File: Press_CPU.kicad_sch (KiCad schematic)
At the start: 97 parts, among them J1 Conn_01x02, J2 2-215079-0, U1 APM32F405RGT6, U10 LMV321, U11 LMV321, U12 FM25W256, U13 LMV321, U14 LMV321, U15 LMV321, U16 LMV321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

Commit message: VER1.0: добавил гребенку
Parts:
- added J3, J4: Conn_01x16, PLD_my:PLD16_2.0mm, symbol Connector_Generic:Conn_01x16
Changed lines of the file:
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@@
+	)
+	(symbol
+		(lib_id "Connector_Generic:Conn_01x16")
+		(at 66.04 214.63 0)
+		(unit 1)
+		(exclude_from_sim no)
+		(in_bom yes)
+		(on_board yes)
+		(dnp no)
+		(fields_autoplaced yes)
+		(property "Reference" "J3"
+			(at 68.58 214.63 0)
+			(effects
+				(font
+					(size 1.27 1.27)
+				)
+				(justify left)
+			)
+		)
+		(property "Value" "Conn_01x16"
+			(at 68.58 217.17 0)
+			(effects
+				(font
+					(size 1.27 1.27)
+				)
+				(justify left)
+			)
+		)
+		(property "Footprint" "PLD_my:PLD16_2.0mm"
+			(at 66.04 214.63 0)
+			(effects
+				(font
+					(size 1.27 1.27)
+				)
+				(hide yes)
+			)
+		)
+		(property "Datasheet" "~"
+			(at 66.04 214.63 0)
+			(effects
+				(font
+					(size 1.27 1.27)
+				)
+				(hide yes)
+			)
+		)
+		(property "Description" "Generic connector, single row, 01x16, script generated (kicad-library-utils/schlib/autogen/connector/)"
+			(at 66.04 214.63 0)
+			(effects
+				(font
+					(size 1.27 1.27)
+				)
+				(hide yes)
+			)
+		)
+		(pin "6"
+		)
+		(pin "9"
+		)
+		(pin "2"
+		)
+		(pin "5"
+		)
+		(pin "14"
+		)
+		(pin "16"
+		)
+		(pin "13"
+		)
+		(pin "1"
+		)
+		(pin "4"
+		)
+		(pin "12"
+		)
+		(pin "15"
+		)
+		(pin "3"
+		)
+		(pin "10"
+		)
+		(pin "7"
+		)
+		(pin "11"
+		)
+		(pin "8"
+		)
+		(instances
+			(project ""
+				(path "/1f44d793-713f-4781-bd7e-20142de81965"
+					(reference "J3")
+					(unit 1)
+				)
+			)
+		)
 	)
 	(symbol
@@
 					(unit 1)
 				)
+			)
+		)
+	)
+	(symbol
+		(lib_id "Connector_Generic:Conn_01x16")
+		(at 83.82 214.63 0)
+		(unit 1)
+		(exclude_from_sim no)
+		(in_bom yes)
+		(on_board yes)
+		(dnp no)
+		(fields_autoplaced yes)
+		(property "Reference" "J4"
+			(at 86.36 214.63 0)
+			(effects
+				(font
+					(size 1.27 1.27)
+				)
+				(justify left)
+			)
+		)
+		(property "Value" "Conn_01x16"
+			(at 86.36 217.17 0)
+			(effects
+				(font
+					(size 1.27 1.27)
+				)
+				(justify left)
+			)
+		)
+		(property "Footprint" "PLD_my:PLD16_2.0mm"
+			(at 83.82 214.63 0)
+			(effects
+				(font
+					(size 1.27 1.27)
+				)
+				(hide yes)
+			)
+		)
+		(property "Datasheet" "~"
+			(at 83.82 214.63 0)
+			(effects
+				(font
+					(size 1.27 1.27)
+				)
+				(hide yes)
+			)
+		)
+		(property "Description" "Generic connector, single row, 01x16, script generated (kicad-library-utils/schlib/autogen/connector/)"
+			(at 83.82 214.63 0)
+			(effects
+				(font
+					(size 1.27 1.27)
+				)
+				(hide yes)
+			)
+		)
+		(pin "6"
+		)
+		(pin "9"
+		)
+		(pin "2"
+		)
+		(pin "5"
+		)
+		(pin "14"
+		)
+		(pin "16"
+		)
+		(pin "13"
+		)
+		(pin "1"
+		)
+		(pin "4"
+		)
+		(pin "12"
+		)
+		(pin "15"
+		)
+		(pin "3"
+		)
+		(pin "10"
+		)
+		(pin "7"
+		)
+		(pin "11"
+		)
+		(pin "8"
+		)
+		(instances
+			(project "Press_CPU"
+				(path "/1f44d793-713f-4781-bd7e-20142de81965"
+					(reference "J4")
+					(unit 1)
+				)

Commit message: VER1.0: добавил в разъём сигналы
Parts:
- removed J1: Conn_01x02, Wire_my:Wire_1.5mm, symbol Connector_Generic:Conn_01x02
- added C40: 1n, Capacitor_SMD:C_0603_1608Metric_Pad1.08x0.95mm_HandSolder, symbol Device:C_Small
- added R37, R66: 3.6k, Resistor_SMD:R_0603_1608Metric_Pad0.98x0.95mm_HandSolder, symbol Device:R_Small
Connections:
- net +5V: now also J3.10 (Pin_10), J4.7 (Pin_7)
- net CANH: now also J2.7
- net CANL: now also J2.6
- net Current_A: now also J3.5 (Pin_5)
- net Current_B: now also J3.4 (Pin_4)
- net Current_C: now also J3.3 (Pin_3)
- net GND: now also J2.11, J2.18, J2.4, J2.9, J3.7 (Pin_7), J3.9 (Pin_9), J4.10 (Pin_10), J4.8 (Pin_8), C40.2, R37.2
- net Hall1: now also J2.1, J4.14 (Pin_14)
- net Hall2: now also J2.2, J4.13 (Pin_13)
- net Hall3: now also J2.5, J4.12 (Pin_12)
- net IN/OUT1: now also J2.12
- net IN/OUT2: now also J2.13
- net IN/OUT3: now also J2.14
- net IN/OUT4: now also J2.15
- net SWCLK: now also J2.19
- net SWDIO: now also J2.20
- net Temp_mosfet_sense: now also J3.2 (Pin_2)
- net Temp_motor_GND: now also J4.15 (Pin_15)
- net Temp_motor_sense: now also J4.16 (Pin_16)
- net VBAT_sense: now also J3.1 (Pin_1)
- net +5V_sense: now reaches J2.10
- net +5V_sense: now also J2.3, J3.6 (Pin_6), J4.11 (Pin_11), R66.1
- net Red_Light+: now reaches J2.16
- net Red_Light-: now reaches J2.17
- net CAN_Power: now reaches J2.8
- net InH1: now reaches J3.11 (Pin_11)
- net PWM1_H: now reaches J3.12 (Pin_12)
- net InH2: now reaches J3.13 (Pin_13)
- net PWM2_H: now reaches J3.14 (Pin_14)
- net InH3: now reaches J3.15 (Pin_15)
- net PWM3_H: now reaches J3.16 (Pin_16)
- net uC_drv_en: now reaches J3.8 (Pin_8)
- net PWM3_L: now reaches J4.1 (Pin_1)
- net InL3: now reaches J4.2 (Pin_2)
- net PWM2_L: now reaches J4.3 (Pin_3)
- net InL2: now reaches J4.4 (Pin_4)
- net PWM1_L: now reaches J4.5 (Pin_5)
- net InL1: now reaches J4.6 (Pin_6)
- net BkIN: now reaches J4.9 (Pin_9)
- new net +5V_sense_MCU: C40.1, R37.1, R66.2
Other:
- note added: "Измерение +5V"
- moved on the sheet: J4

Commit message: VER1.0: промежуточная трассировка
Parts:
- removed C3: 56p, Capacitor_SMD:C_0603_1608Metric_Pad1.08x0.95mm_HandSolder, symbol Device:C_Small
- added C18: 10u, Capacitor_SMD:C_0805_2012Metric_Pad1.18x1.45mm_HandSolder, symbol Device:C_Small
- C17: footprint Capacitor_SMD:C_1210_3225Metric_Pad1.33x2.70mm_HandSolder -> Capacitor_SMD:C_0805_2012Metric_Pad1.18x1.45mm_HandSolder
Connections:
- net InH1 is gone; now on net PWM1_H: J3.11 (Pin_11)
- net InH2 is gone; now on net PWM2_H: J3.13 (Pin_13)
- net InH3 is gone; now on net PWM3_H: J3.15 (Pin_15)
- net InL1 is gone; now on net PWM1_L: J4.6 (Pin_6)
- net InL2 is gone; now on net PWM2_L: J4.4 (Pin_4)
- net InL3 is gone; now on net PWM3_L: J4.2 (Pin_2)
- net +5V: now also C18.1; no longer R65.1
- net +5V_sense: now also R65.1
- net ADC10: no longer U1.21 (PA5)
- net ADC11: no longer U1.22 (PA6)
- net ADC12: no longer U1.23 (PA7)
- net ADC9: no longer U1.20 (PA4)
- net BkIN: now also U1.33 (PB12)
- net CAN1_RXD_MCU: now also U1.61 (PB8); no longer U1.44 (PA11)
- net CAN1_TXD_MCU: now also U1.62 (PB9); no longer U1.45 (PA12)
- net EEPROM_MISO_MCU: now also U1.22 (PA6); no longer U1.35 (PB14)
- net EEPROM_MOSI_MCU: now also U1.23 (PA7); no longer U1.36 (PB15)
- net EEPROM_SCK_MCU: now also U1.21 (PA5); no longer U1.34 (PB13)
- net EEPROM_~{CS_MCU}: now also U1.20 (PA4); no longer U1.33 (PB12)
- net GND: now also C18.2
- net PWM1_H: now also U1.41 (PA8); no longer J3.12 (Pin_12)
- net PWM1_L: now also U1.34 (PB13); no longer J4.5 (Pin_5)
- net PWM2_H: now also U1.42 (PA9); no longer J3.14 (Pin_14)
- net PWM2_L: now also U1.35 (PB14); no longer J4.3 (Pin_3)
- net PWM3_H: now also U1.43 (PA10); no longer J3.16 (Pin_16)
- net PWM3_L: now also U1.36 (PB15); no longer J4.1 (Pin_1)
- net uC_drv_en: now also U1.58 (PB6)
- net f3L: now reaches U1.37 (PC6)
- net f3L: now also J4.1 (Pin_1)
- net f3H: now reaches U1.38 (PC7)
- net f3H: now also J3.16 (Pin_16)
- net f2H: now reaches U1.39 (PC8)
- net f2H: now also J3.14 (Pin_14)
- net f2L: now reaches U1.40 (PC9)
- net f2L: now also J4.3 (Pin_3)
- new net f1H: J3.12 (Pin_12), U1.44 (PA11)
- new net f1L: J4.5 (Pin_5), U1.45 (PA12)

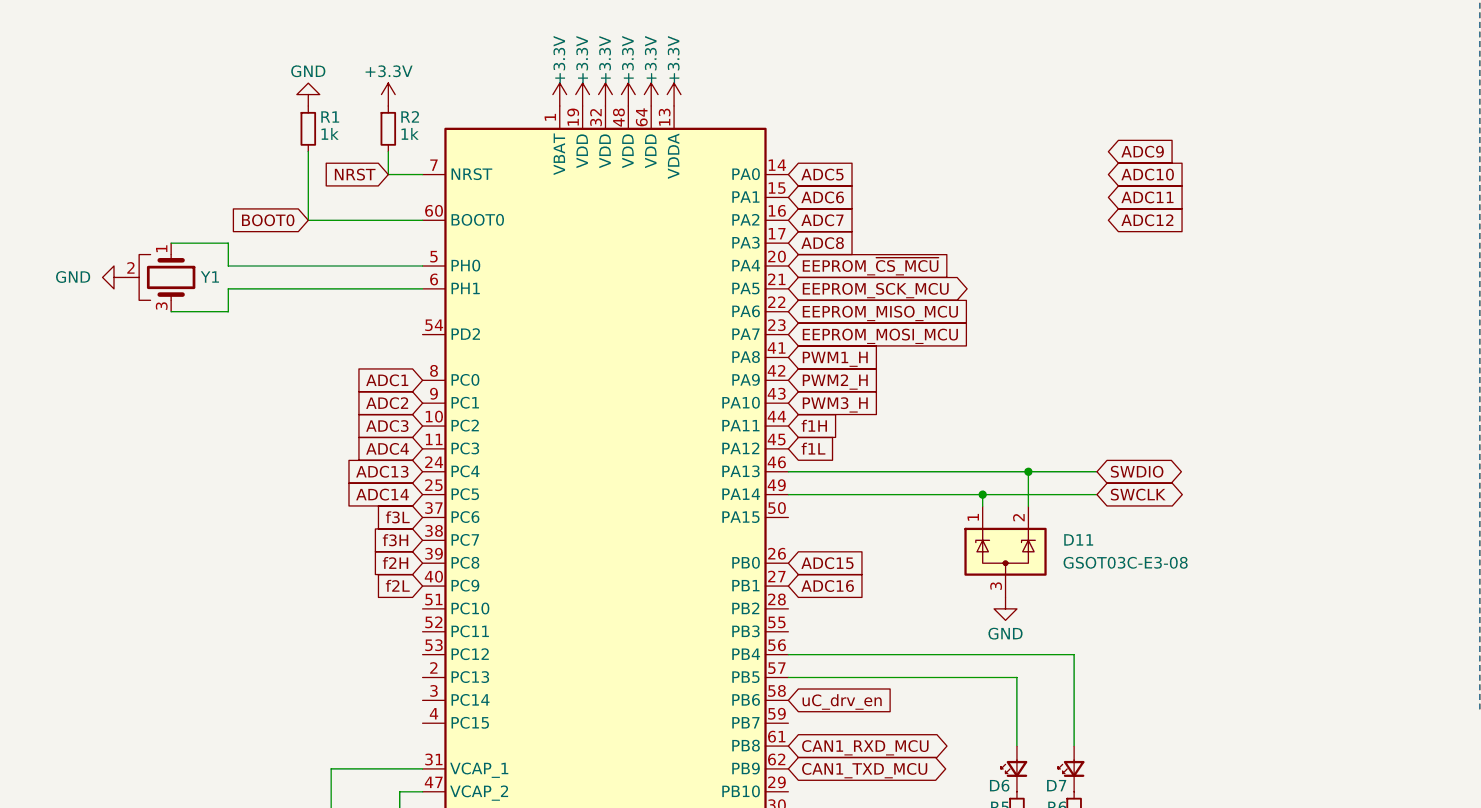
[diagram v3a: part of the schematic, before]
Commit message: VER1.0: проблема с пересечением EEPROM и аналоговыми входами
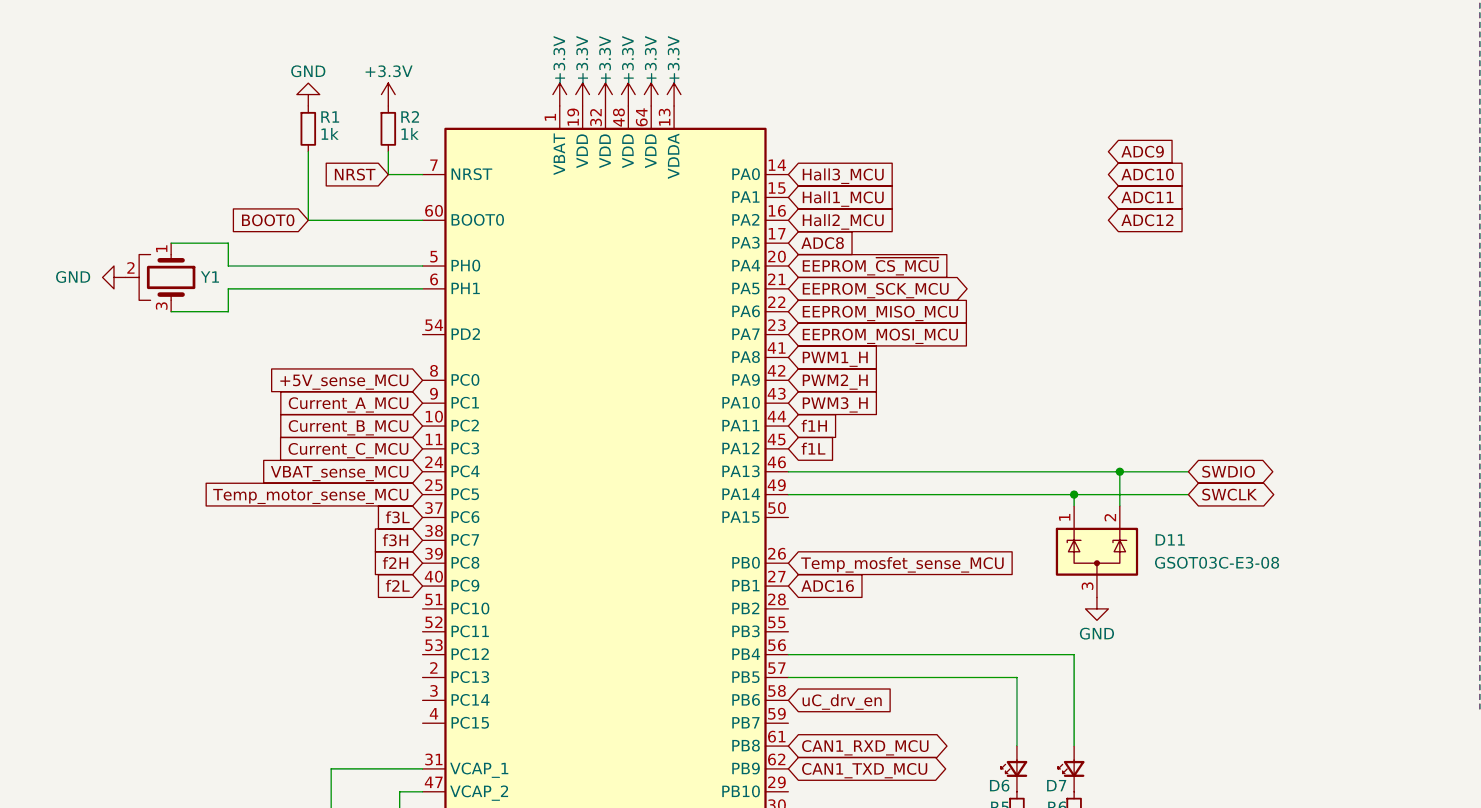
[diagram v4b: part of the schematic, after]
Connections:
- net ADC1 is gone; now on net +5V_sense_MCU: U1.8 (PC0)
- net ADC13 is gone; now on net VBAT_sense_MCU: U1.24 (PC4)
- net ADC14 is gone; now on net Temp_motor_sense_MCU: U1.25 (PC5)
- net ADC15 is gone; now on net Temp_mosfet_sense_MCU: U1.26 (PB0)
- net ADC2 is gone; now on net Current_A_MCU: U1.9 (PC1)
- net ADC3 is gone; now on net Current_B_MCU: U1.10 (PC2)
- net ADC4 is gone; now on net Current_C_MCU: U1.11 (PC3)
- net ADC5 is gone; now on net Hall3_MCU: U1.14 (PA0)
- net ADC6 is gone; now on net Hall1_MCU: U1.15 (PA1)
- net ADC7 is gone; now on net Hall2_MCU: U1.16 (PA2)
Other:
- moved on the sheet: D11

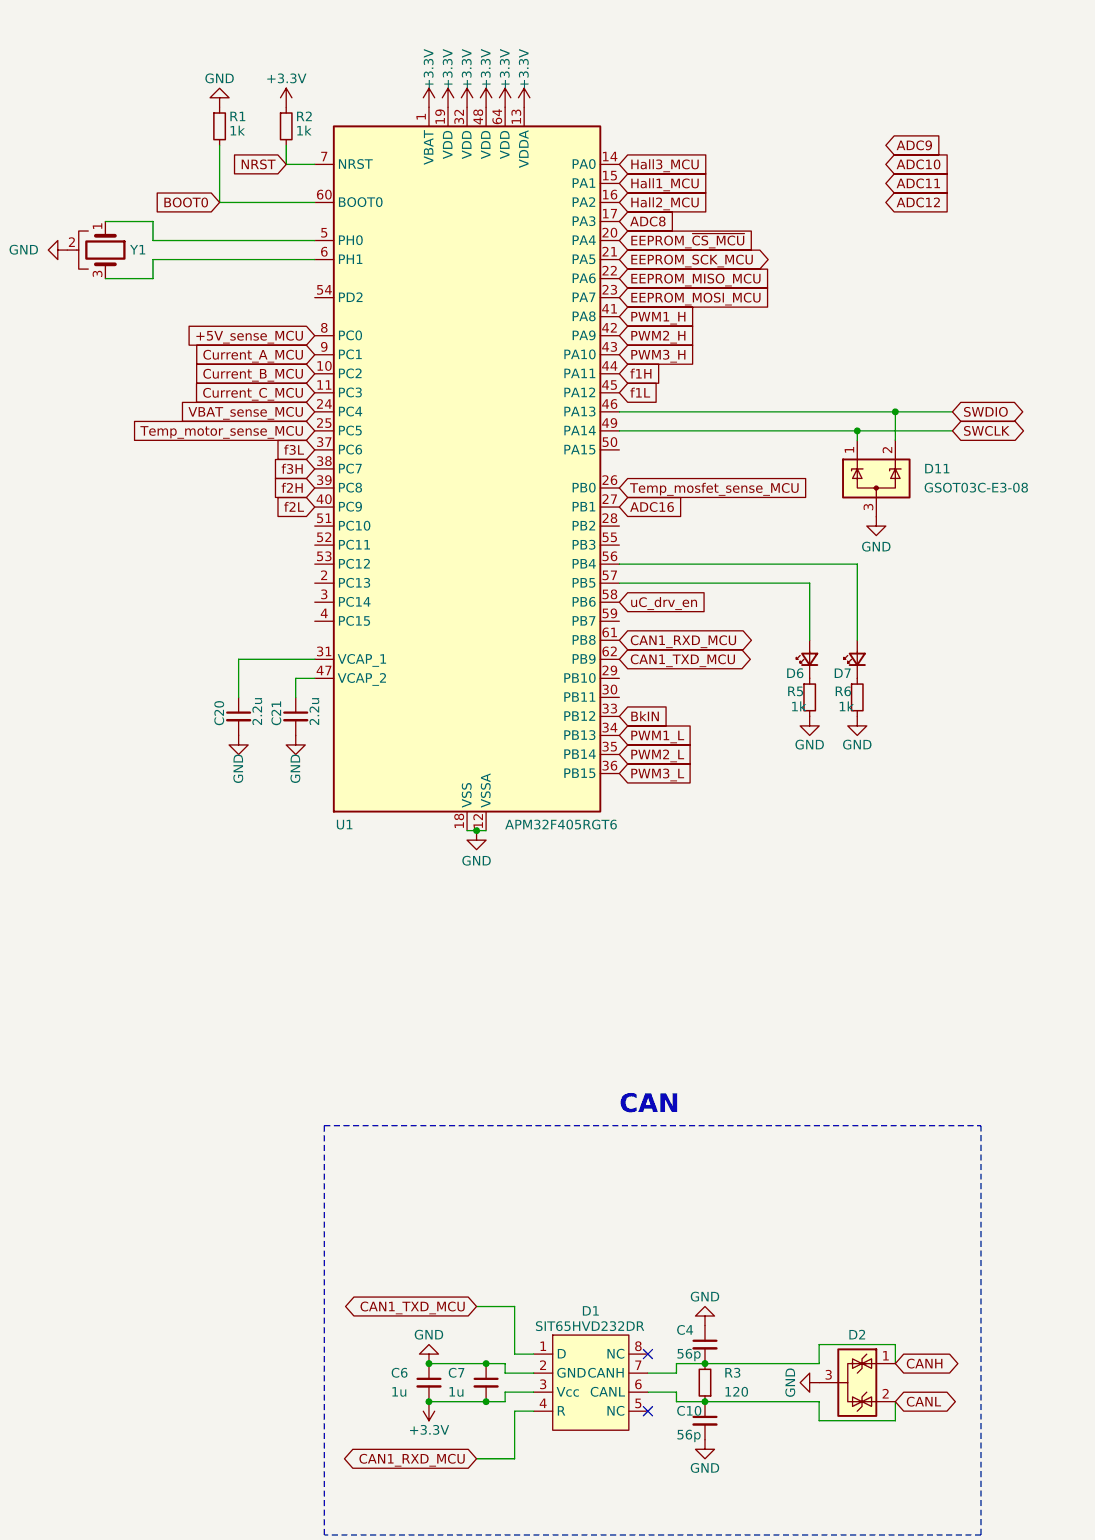
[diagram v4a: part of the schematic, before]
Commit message: VER1.0: попробовал развести по другому
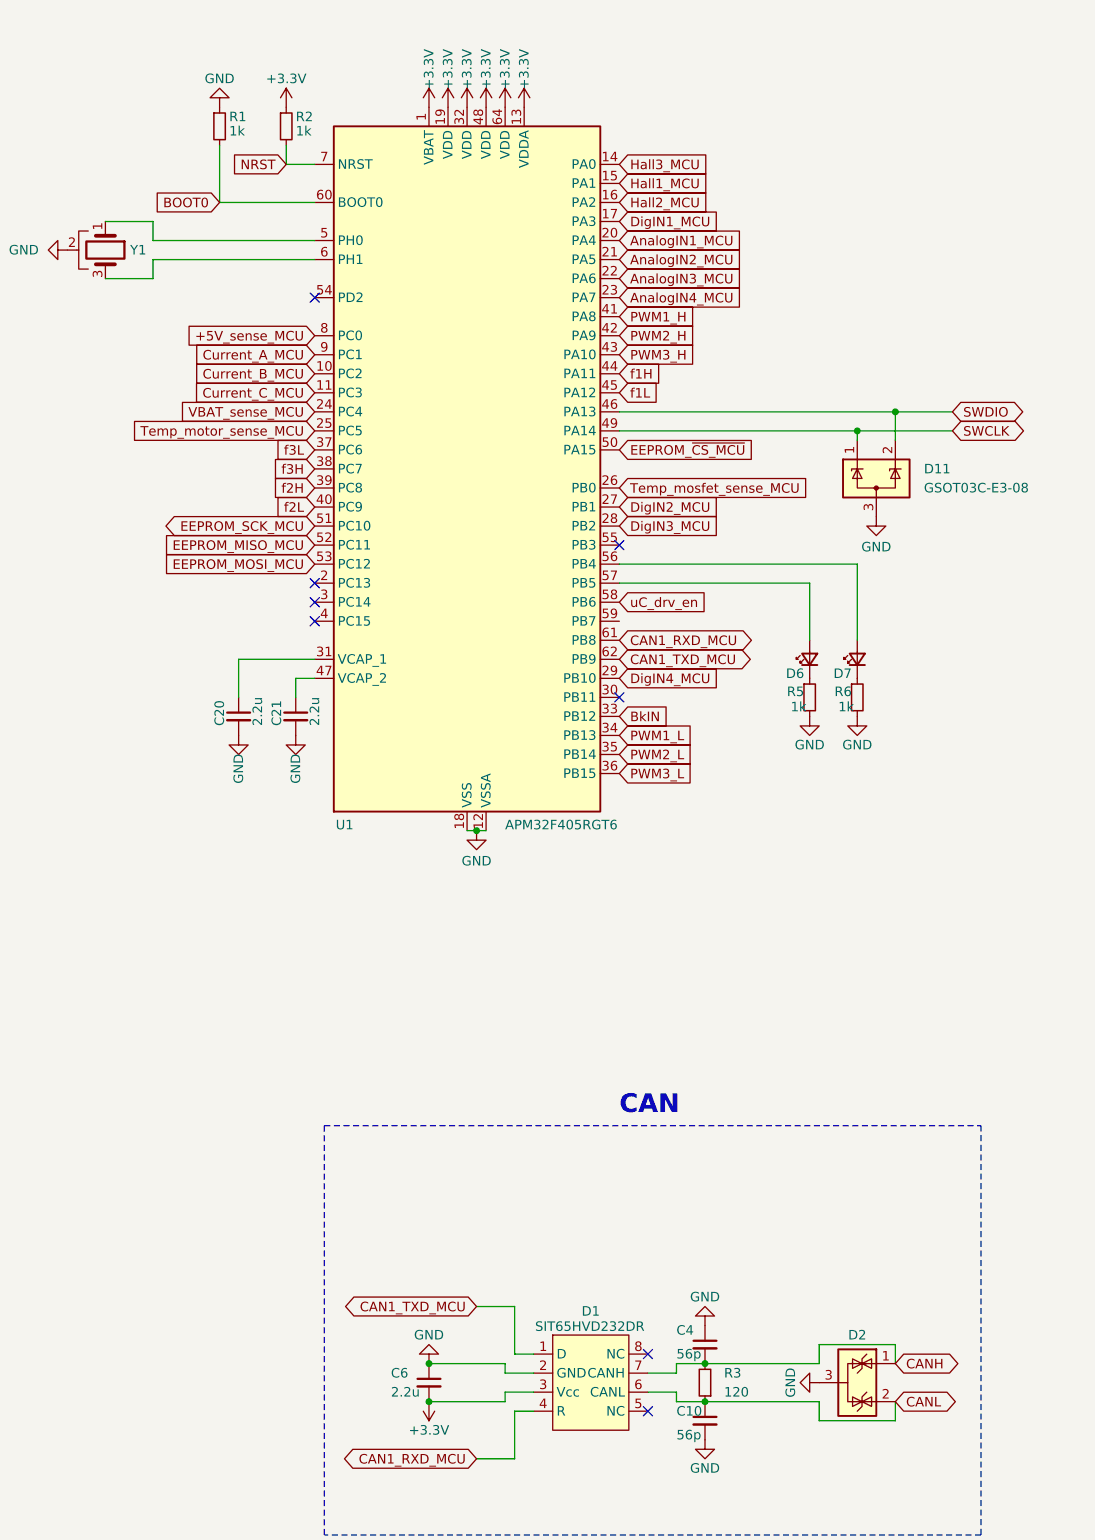
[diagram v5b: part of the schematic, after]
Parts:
- removed C7: 1u, Capacitor_SMD:C_0603_1608Metric_Pad1.08x0.95mm_HandSolder, symbol Device:C_Small
- C6: value 1u -> 2.2u
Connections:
- net ADC16 is gone; now on net DigIN2_MCU: U1.27 (PB1)
- net ADC8 is gone; now on net DigIN1_MCU: U1.17 (PA3)
- net AnalogIN1_MCU: now also U1.20 (PA4)
- net AnalogIN2_MCU: now also U1.21 (PA5)
- net AnalogIN3_MCU: now also U1.22 (PA6)
- net AnalogIN4_MCU: now also U1.23 (PA7)
- net DigIN3_MCU: now also U1.28 (PB2)
- net DigIN4_MCU: now also U1.29 (PB10)
- net EEPROM_MISO_MCU: now also U1.52 (PC11); no longer U1.22 (PA6)
- net EEPROM_MOSI_MCU: now also U1.53 (PC12); no longer U1.23 (PA7)
- net EEPROM_SCK_MCU: now also U1.51 (PC10); no longer U1.21 (PA5)
- net EEPROM_~{CS_MCU}: now also U1.50 (PA15); no longer U1.20 (PA4)
- no-connect marks 5 -> 11
